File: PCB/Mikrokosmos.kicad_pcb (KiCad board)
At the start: 2 copper layers, 81.5 x 25 mm, 20 parts, among them J1 EURO_PWR_2x5, J4 Molex 2 pin, J5 Molex 2 pin, U2 TL072

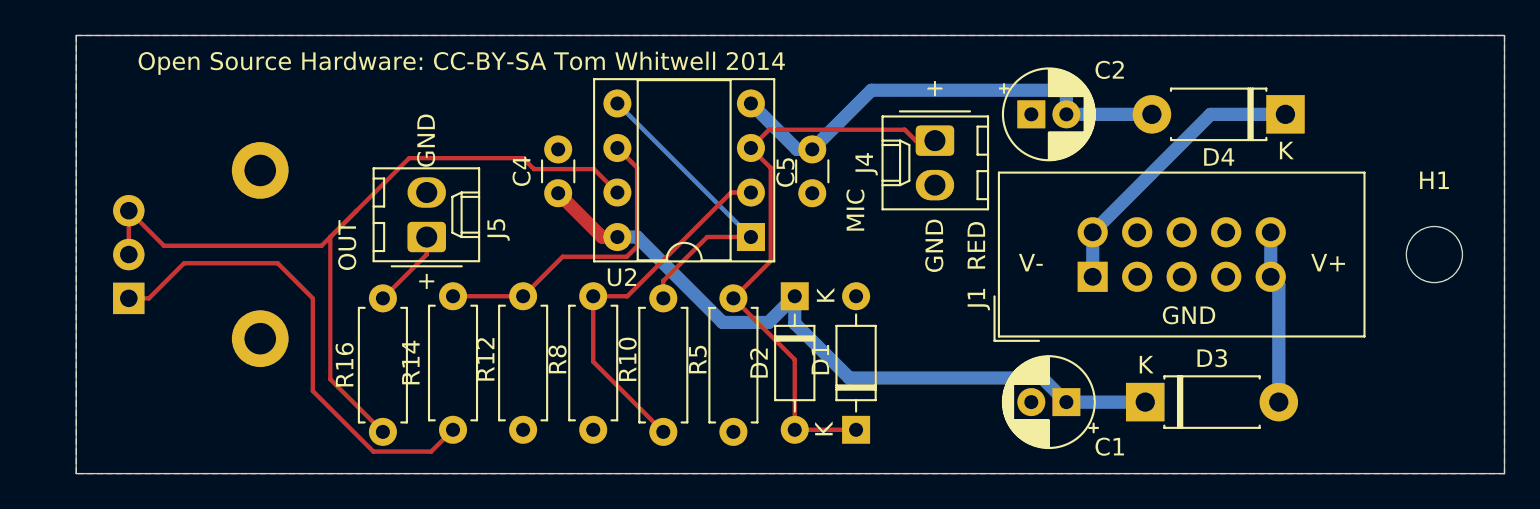
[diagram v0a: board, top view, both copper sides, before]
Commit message: Connect plane to ground via jacks
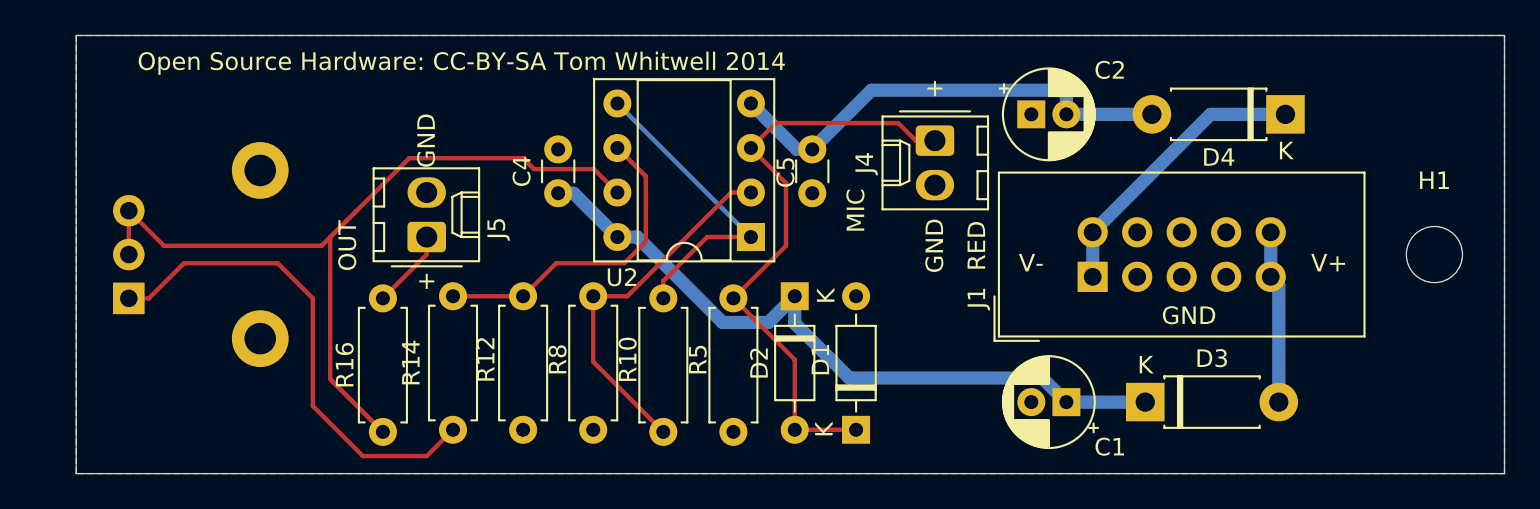
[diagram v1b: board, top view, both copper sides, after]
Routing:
- net /MIC+: track 34.2 -> 35.2 mm
- net Net-(R14-Pad1): track 27.4 -> 28.1 mm
- net Net-(R12-Pad1): track 17.8 -> 18.3 mm
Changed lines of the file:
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@@
       (drillshape 0)
       (scaleselection 1)
-      (outputdirectory ""))
+      (outputdirectory "Gerbers/"))
   )
   (net 0 "")
@@
   (segment (start 139.51137 111.5) (end 144.386371 116.375001) (width 0.75) (layer B.Cu) (net 2))
   (segment (start 138.38 111.5) (end 139.51137 111.5) (width 0.75) (layer B.Cu) (net 2) (status 10))
-  (segment (start 137.5 111.5) (end 135 109) (width 0.75) (layer F.Cu) (net 2) (status 20))
-  (segment (start 138.38 111.5) (end 137.5 111.5) (width 0.75) (layer F.Cu) (net 2) (status 10))
   (segment (start 148.5 116.43) (end 148.5 114.88) (width 0.75) (layer B.Cu) (net 2) (status 20))
   (segment (start 151.614999 119.544999) (end 148.5 116.43) (width 0.75) (layer B.Cu) (net 2))
   (segment (start 162.624999 119.544999) (end 151.614999 119.544999) (width 0.75) (layer B.Cu) (net 2))
   (segment (start 164 120.92) (end 162.624999 119.544999) (width 0.75) (layer B.Cu) (net 2) (status 10))
+  (segment (start 135.88 109) (end 138.38 111.5) (width 0.75) (layer B.Cu) (net 2))
+  (segment (start 135 109) (end 135.88 109) (width 0.75) (layer B.Cu) (net 2))
   (segment (start 168.88 104.5) (end 164 104.5) (width 0.75) (layer B.Cu) (net 3) (status 30))
   (segment (start 148.62 106.5) (end 146 103.88) (width 0.75) (layer B.Cu) (net 3) (status 20))
@@
   (segment (start 141 114) (end 143.5 111.5) (width 0.25) (layer F.Cu) (net 6))
   (segment (start 129 114.88) (end 133 114.88) (width 0.25) (layer F.Cu) (net 7))
+  (segment (start 140 111.772501) (end 140 108.04) (width 0.25) (layer F.Cu) (net 7))
+  (segment (start 140 108.04) (end 139.179999 107.219999) (width 0.25) (layer F.Cu) (net 7))
+  (segment (start 138.772501 113) (end 140 111.772501) (width 0.25) (layer F.Cu) (net 7))
   (segment (start 139.179999 107.219999) (end 138.38 106.42) (width 0.25) (layer F.Cu) (net 7))
-  (segment (start 139.505001 107.545001) (end 139.179999 107.219999) (width 0.25) (layer F.Cu) (net 7))
-  (segment (start 139.505001 112.040001) (end 139.505001 107.545001) (width 0.25) (layer F.Cu) (net 7))
-  (segment (start 138.920001 112.625001) (end 139.505001 112.040001) (width 0.25) (layer F.Cu) (net 7))
-  (segment (start 135.254999 112.625001) (end 138.920001 112.625001) (width 0.25) (layer F.Cu) (net 7))
-  (segment (start 133 114.88) (end 135.254999 112.625001) (width 0.25) (layer F.Cu) (net 7))
+  (segment (start 133 114.88) (end 134.88 113) (width 0.25) (layer F.Cu) (net 7))
+  (segment (start 134.88 113) (end 138.772501 113) (width 0.25) (layer F.Cu) (net 7))
+  (segment (start 111.65 115) (end 110.5 115) (width 0.25) (layer F.Cu) (net 8))
+  (segment (start 127.5 124) (end 123.857499 124) (width 0.25) (layer F.Cu) (net 8))
+  (segment (start 129 122.5) (end 127.5 124) (width 0.25) (layer F.Cu) (net 8))
   (segment (start 113.65 113) (end 111.65 115) (width 0.25) (layer F.Cu) (net 8))
-  (segment (start 111.65 115) (end 110.5 115) (width 0.25) (layer F.Cu) (net 8))
-  (segment (start 124.459999 123.745001) (end 121 120.285002) (width 0.25) (layer F.Cu) (net 8))
-  (segment (start 129 122.5) (end 127.754999 123.745001) (width 0.25) (layer F.Cu) (net 8))
-  (segment (start 127.754999 123.745001) (end 124.459999 123.745001) (width 0.25) (layer F.Cu) (net 8))
+  (segment (start 123.857499 124) (end 121 121.142501) (width 0.25) (layer F.Cu) (net 8))
+  (segment (start 121 121.142501) (end 121 115) (width 0.25) (layer F.Cu) (net 8))
   (segment (start 121 115) (end 119 113) (width 0.25) (layer F.Cu) (net 8))
-  (segment (start 121 120.285002) (end 121 115) (width 0.25) (layer F.Cu) (net 8))
   (segment (start 119 113) (end 113.65 113) (width 0.25) (layer F.Cu) (net 8))
   (segment (start 110.5 110.005) (end 110.5 112.505) (width 0.25) (layer F.Cu) (net 9) (status 30))
@@
   (segment (start 148.5 118.5) (end 148.5 122.5) (width 0.25) (layer F.Cu) (net 11) (status 20))
   (segment (start 145 115) (end 148.5 118.5) (width 0.25) (layer F.Cu) (net 11) (status 10))
-  (segment (start 147.125001 107.545001) (end 146 106.42) (width 0.25) (layer F.Cu) (net 11) (status 20))
-  (segment (start 147.125001 112.874999) (end 147.125001 107.545001) (width 0.25) (layer F.Cu) (net 11))
-  (segment (start 145 115) (end 147.125001 112.874999) (width 0.25) (layer F.Cu) (net 11) (status 10))
-  (segment (start 155.4 106) (end 156.5 106) (width 0.25) (layer F.Cu) (net 11) (status 30))
-  (segment (start 154.774999 105.374999) (end 155.4 106) (width 0.25) (layer F.Cu) (net 11) (status 20))
-  (segment (start 147.045001 105.374999) (end 154.774999 105.374999) (width 0.25) (layer F.Cu) (net 11))
-  (segment (start 146 106.42) (end 147.045001 105.374999) (width 0.25) (layer F.Cu) (net 11) (status 10))
+  (segment (start 148 108.42) (end 146 106.42) (width 0.25) (layer F.Cu) (net 11))
+  (segment (start 145 115) (end 148 112) (width 0.25) (layer F.Cu) (net 11))
+  (segment (start 148 112) (end 148 108.42) (width 0.25) (layer F.Cu) (net 11))
+  (segment (start 155.4 106) (end 156.5 106) (width 0.25) (layer F.Cu) (net 11))
+  (segment (start 154.4 105) (end 155.4 106) (width 0.25) (layer F.Cu) (net 11))
+  (segment (start 146 106.42) (end 147.42 105) (width 0.25) (layer F.Cu) (net 11))
+  (segment (start 147.42 105) (end 154.4 105) (width 0.25) (layer F.Cu) (net 11))
   (segment (start 165.5 113.77) (end 165.5 111.23) (width 0.75) (layer B.Cu) (net 12) (status 30))
   (segment (start 172.23 104.5) (end 176.5 104.5) (width 0.75) (layer B.Cu) (net 12) (status 20))
